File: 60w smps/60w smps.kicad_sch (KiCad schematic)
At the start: 37 parts, among them J1 Screw_Terminal_01x02, J2 Screw_Terminal_01x02, Q1 2N7000, T1 Transformer_1P_1S, U1 UC3842_DIP8

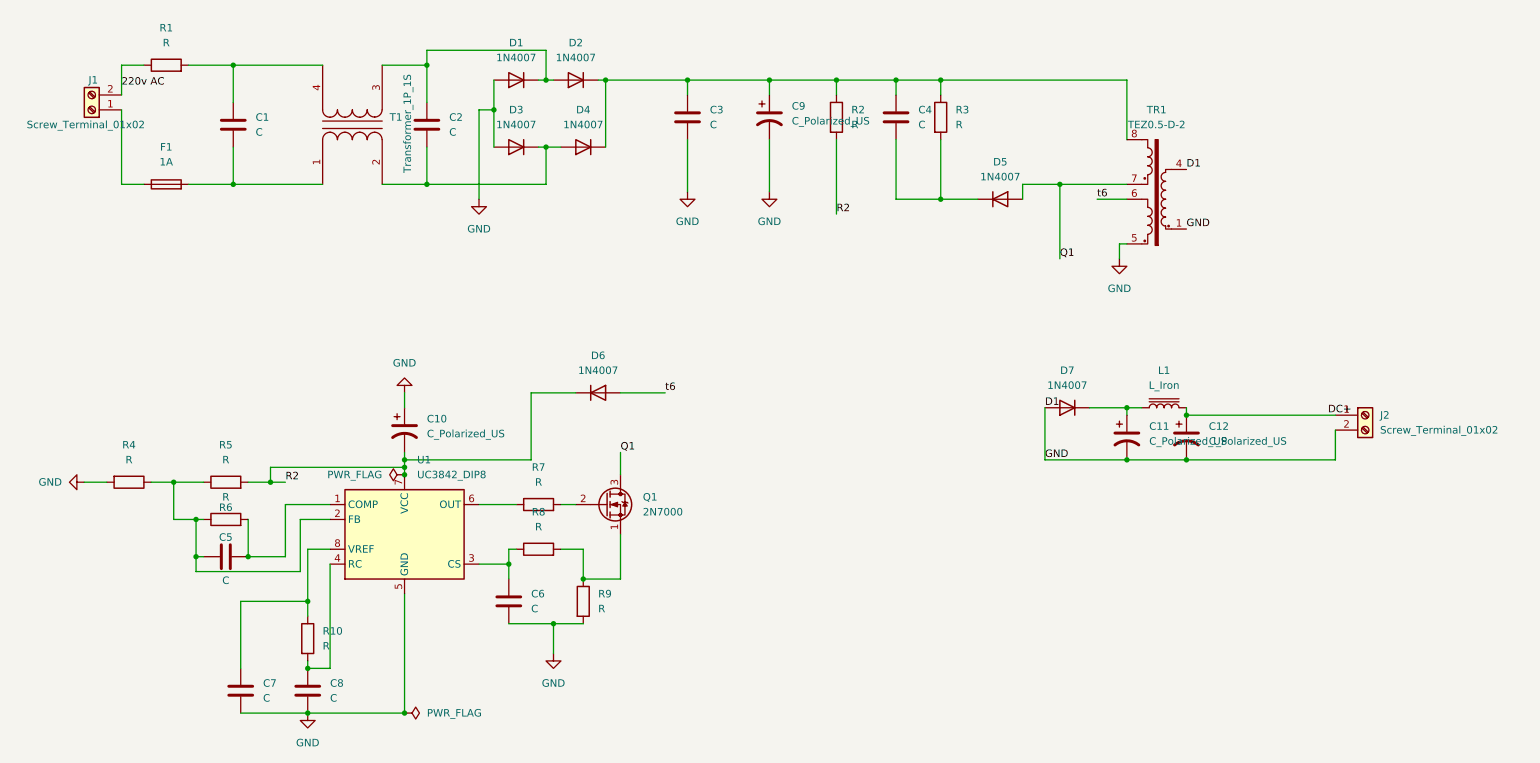
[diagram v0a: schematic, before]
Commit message: untrack .history pointers and lock files, add new projects
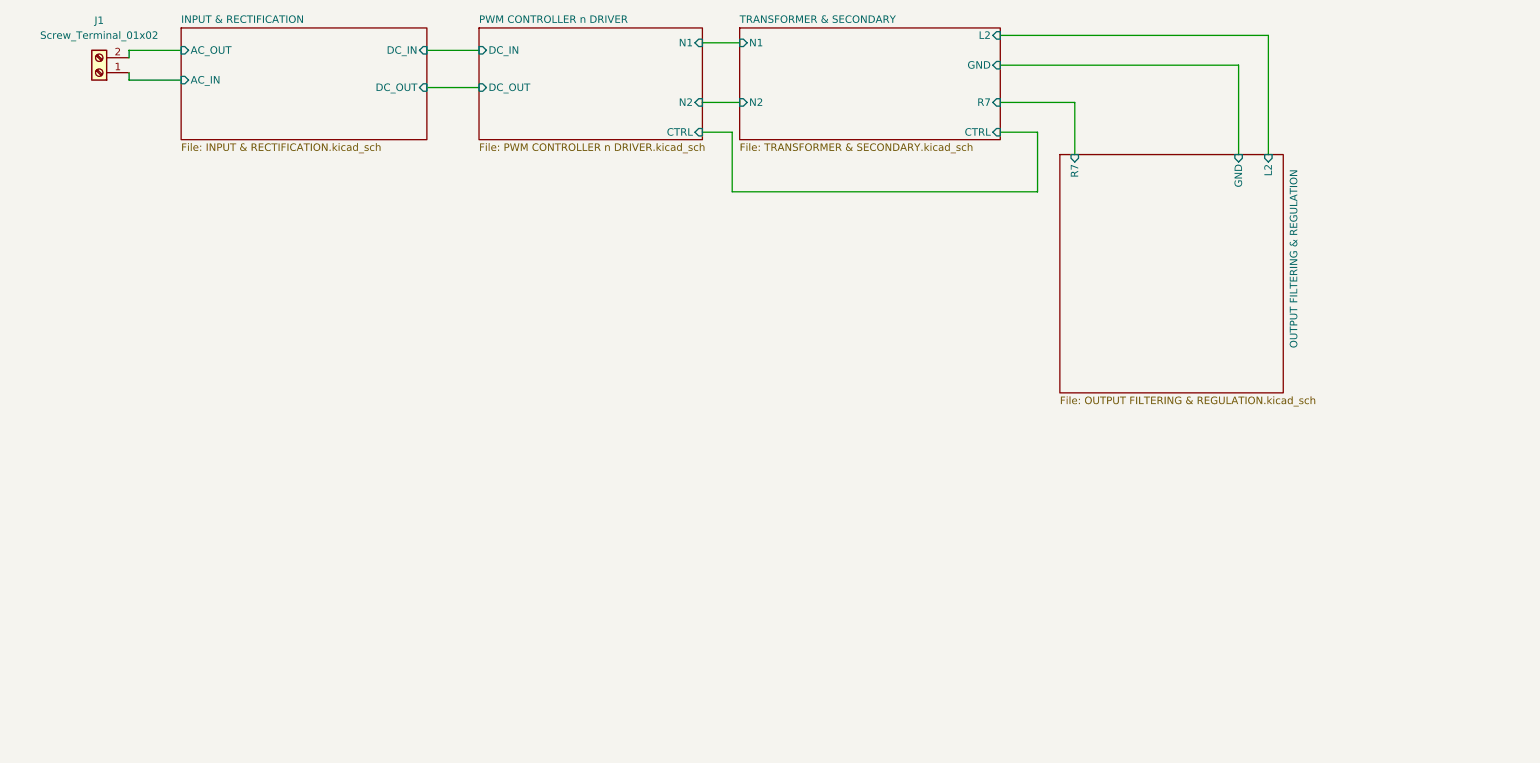
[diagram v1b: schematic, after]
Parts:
- removed C1, C2, C3, C4, C5, C6, C7, C8: C, Capacitor_THT:CP_Radial_D7.5mm_P2.50mm, symbol Device:C
- removed C10, C11, C12, C9: C_Polarized_US, Capacitor_THT:CP_Axial_L10.0mm_D4.5mm_P15.00mm_Horizontal, symbol Device:C_Polarized_US
- removed D1, D2, D3, D4, D5, D6, D7: 1N4007, Diode_THT:D_DO-41_SOD81_P10.16mm_Horizontal, symbol Diode:1N4007
- removed F1: 1A, Fuse:Fuse_Littelfuse-LVR125, symbol Device:Fuse
- removed J2: Screw_Terminal_01x02, TerminalBlock:TerminalBlock_MaiXu_MX126-5.0-02P_1x02_P5.00mm, symbol Connector:Screw_Terminal_01x02
- removed L1: L_Iron, Inductor_THT:L_Axial_L5.0mm_D3.6mm_P10.00mm_Horizontal_Murata_BL01RN1A2A2, symbol Device:L_Iron
- removed Q1: 2N7000, Package_TO_SOT_THT:TO-92_Inline, symbol Transistor_FET:2N7000
- removed R1, R10, R2, R4, R6, R8: R, Resistor_THT:R_Axial_DIN0204_L3.6mm_D1.6mm_P1.90mm_Vertical, symbol Device:R
- removed R3, R5, R7, R9: R, Resistor_SMD:R_0201_0603Metric, symbol Device:R
- removed T1: Transformer_1P_1S, Transformer_THT:Transformer_NF_ETAL_1-1_P1200, symbol Device:Transformer_1P_1S
- removed TR1: TEZ0.5-D-2, Transformer_THT:Transformer_Breve_TEZ-22x24, symbol Transformer:TEZ0.5-D-2
- removed U1: UC3842_DIP8, Package_DIP:DIP-8_W7.62mm, symbol Regulator_Controller:UC3842_DIP8
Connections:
- net INPUT & RECTIFICATION/AC_IN: now reaches J1.1 (Pin_1)
- net 220v AC renamed INPUT & RECTIFICATION/AC_OUT
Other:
- added sheet INPUT & RECTIFICATION (INPUT & RECTIFICATION.kicad_sch)
- added sheet OUTPUT FILTERING & REGULATION (OUTPUT FILTERING & REGULATION.kicad_sch)
- added sheet PWM CONTROLLER n DRIVER (PWM CONTROLLER n DRIVER.kicad_sch)
- added sheet TRANSFORMER & SECONDARY (TRANSFORMER & SECONDARY.kicad_sch)
- company: Rudra  -> (none)
- title: 60w smps -> (none)
